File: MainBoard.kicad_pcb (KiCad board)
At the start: 4 copper layers, 150 x 100 mm, 143 parts, among them IC2 STUSB4500LQTR, IC3 RT8293BHZSP, IC4 RT8293BHZSP, J15 USB_C_2.0, J4 Conn_01x06_Pin, J7 IEC61076-2_M8_B-coding_01x03_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, Q6 STL9P3LLH6, Q7 STL9P3LLH6, U1 STM32H723ZGT6, U27 USBLC6-2P6, U4 CA-IS2062W, U51 24AA02-OT, Y5 12M, Y6 32,768kHz

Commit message: I/O Schematic rebuild from DRAFT by Nathann
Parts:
- added C156: 10u/25V/X5R, Capacitor_SMD:C_0805_2012Metric, F.Cu at (83.1, 110.4)
- added L16: 1u/5A, Inductor_SMD:L_APV_APH0650, F.Cu at (80.3, 116.0)
- added U10: VND7050AJTR, Package_SO:PowerSSO-16-1EP_3.9x4.9mm_P0.5mm_EP2.5x3.61mm, F.Cu at (252.6, 58.1)
- added U11: VND7050AJTR, Package_SO:PowerSSO-16-1EP_3.9x4.9mm_P0.5mm_EP2.5x3.61mm, F.Cu at (252.6, 64.5)
- added U12: VND7050AJTR, Package_SO:PowerSSO-16-1EP_3.9x4.9mm_P0.5mm_EP2.5x3.61mm, F.Cu at (252.6, 71.0)
- added U13: VND7050AJTR, Package_SO:PowerSSO-16-1EP_3.9x4.9mm_P0.5mm_EP2.5x3.61mm, F.Cu at (252.6, 77.4)
- added U14: VND7050AJTR, Package_SO:PowerSSO-16-1EP_3.9x4.9mm_P0.5mm_EP2.5x3.61mm, F.Cu at (252.6, 83.9)
- added U15: VND7050AJTR, Package_SO:PowerSSO-16-1EP_3.9x4.9mm_P0.5mm_EP2.5x3.61mm, F.Cu at (273.3, 58.1)
- added U3: VND7050AJTR, Package_SO:PowerSSO-16-1EP_3.9x4.9mm_P0.5mm_EP2.5x3.61mm, F.Cu at (262.9, 51.6)
- added U5: VND7050AJTR, Package_SO:PowerSSO-16-1EP_3.9x4.9mm_P0.5mm_EP2.5x3.61mm, F.Cu at (262.9, 58.1)
- added U6: VND7050AJTR, Package_SO:PowerSSO-16-1EP_3.9x4.9mm_P0.5mm_EP2.5x3.61mm, F.Cu at (262.9, 64.5)
- added U7: VND7050AJTR, Package_SO:PowerSSO-16-1EP_3.9x4.9mm_P0.5mm_EP2.5x3.61mm, F.Cu at (262.9, 71.0)
- added U8: VND7050AJTR, Package_SO:PowerSSO-16-1EP_3.9x4.9mm_P0.5mm_EP2.5x3.61mm, F.Cu at (273.3, 51.6)
- added U9: VND7050AJTR, Package_SO:PowerSSO-16-1EP_3.9x4.9mm_P0.5mm_EP2.5x3.61mm, F.Cu at (252.6, 51.6)
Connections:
- net /USB_PD/USB_N renamed /MCU/USB_N
- net /USB_PD/USB_P renamed /MCU/USB_P
- net /USB_PD/USB_PD_ALERT renamed /MCU/USB_PD_ALERT
- net /USB_PD/USB_PD_RST renamed /MCU/USB_PD_RST
- C134 pad 1: +12V -> Net-(IC3-VIN)
- C269 pad 1: unconnected-(C269-Pad1) -> Net-(U1PortG_PORTH-PC15)
- C270 pad 1: unconnected-(C270-Pad1) -> Net-(U1PortG_PORTH-PC14)
- IC2 pad 7: /USB_PD/I2C2.SCK -> /MCU/I2C2.SCK
- IC2 pad 8: /USB_PD/I2C2.DATA -> /MCU/I2C2.DATA
- IC3 pad 2: +12V -> Net-(IC3-VIN)
- L15 pad 2: +5V -> +12V
- R148 pad 1: +12V -> Net-(IC3-VIN)
- TP22 pad 1: /USB_PD/I2C2.SCK -> /MCU/I2C2.SCK
- TP23 pad 1: /USB_PD/I2C2.DATA -> /MCU/I2C2.DATA
- U1 pad 8: unconnected-(U1PortG_PORTH-PC14-Pad8) -> Net-(U1PortG_PORTH-PC14)
- U1 pad 9: unconnected-(U1PortG_PORTH-PC15-Pad9) -> Net-(U1PortG_PORTH-PC15)
- U4 pad 3: unconnected-(U4-TX-Pad3) -> /PowertrainInterface/CAN1.TX
- U4 pad 5: unconnected-(U4-RX-Pad5) -> /PowertrainInterface/CAN1.RX
- Y6 pad 1: unconnected-(Y6-Pad1) -> Net-(U1PortG_PORTH-PC15)
- Y6 pad 2: unconnected-(Y6-Pad2) -> Net-(U1PortG_PORTH-PC14)
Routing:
- net /MCU/I2C2.DATA: track 19.4 -> 38.0 mm, vias 2 -> 3
- net /USB_PD/I2C2.DATA: track 18.6 -> 0.00 mm, vias 1 -> 0
- net (no net): track 33.4 -> 16.8 mm
- net /USB_PD/I2C2.SCK: track 16.2 -> 0.00 mm, vias 1 -> 0
- net /MCU/I2C2.SCK: track 13.7 -> 29.9 mm, vias 2 -> 3
- net Net-(U1PortG_PORTH-PC15): track 0.00 -> 8.46 mm
- net Net-(U1PortG_PORTH-PC14): track 0.00 -> 8.21 mm
- net Net-(IC3-VIN): track 0.00 -> 4.23 mm, vias 0 -> 1
- net +5V: track 26.3 -> 23.1 mm
- net +12V: track 4.23 -> 3.16 mm, vias 1 -> 0

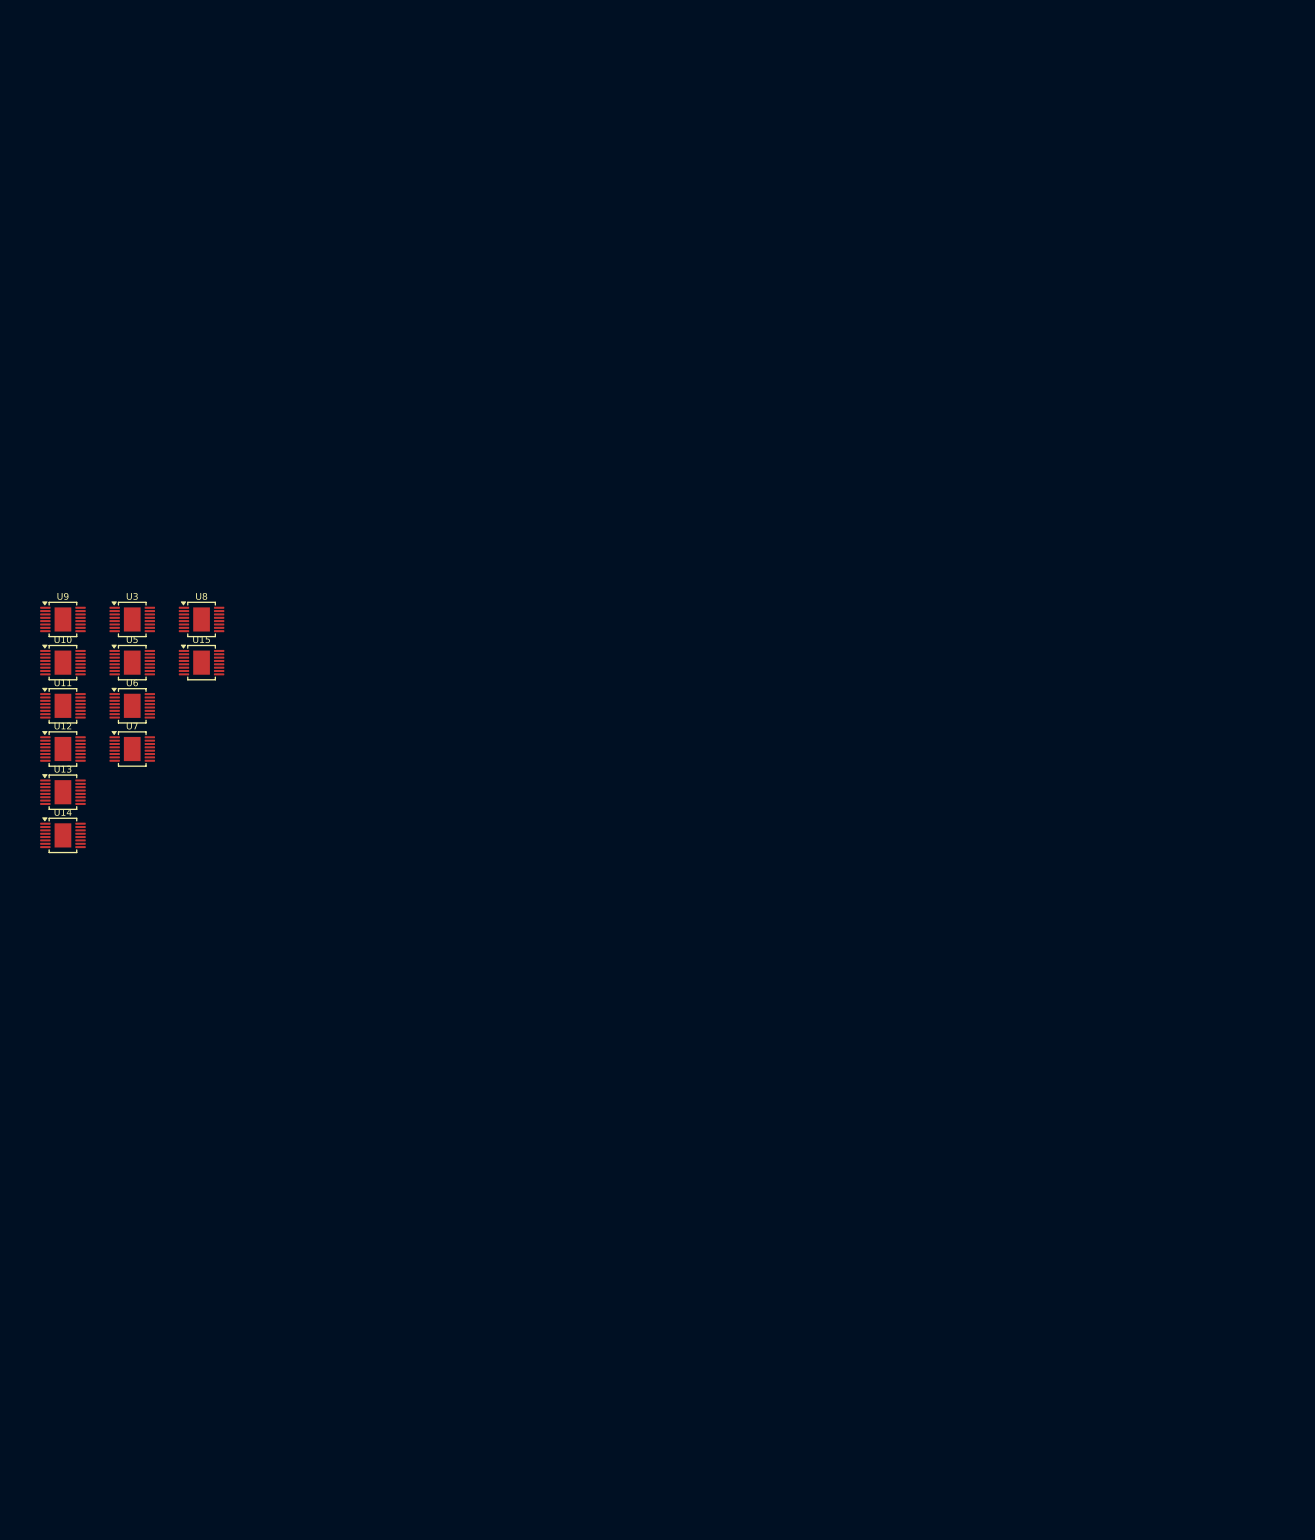
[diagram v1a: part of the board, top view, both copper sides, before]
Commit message: EMI/EMC meassures implementation + VCU panel interface block
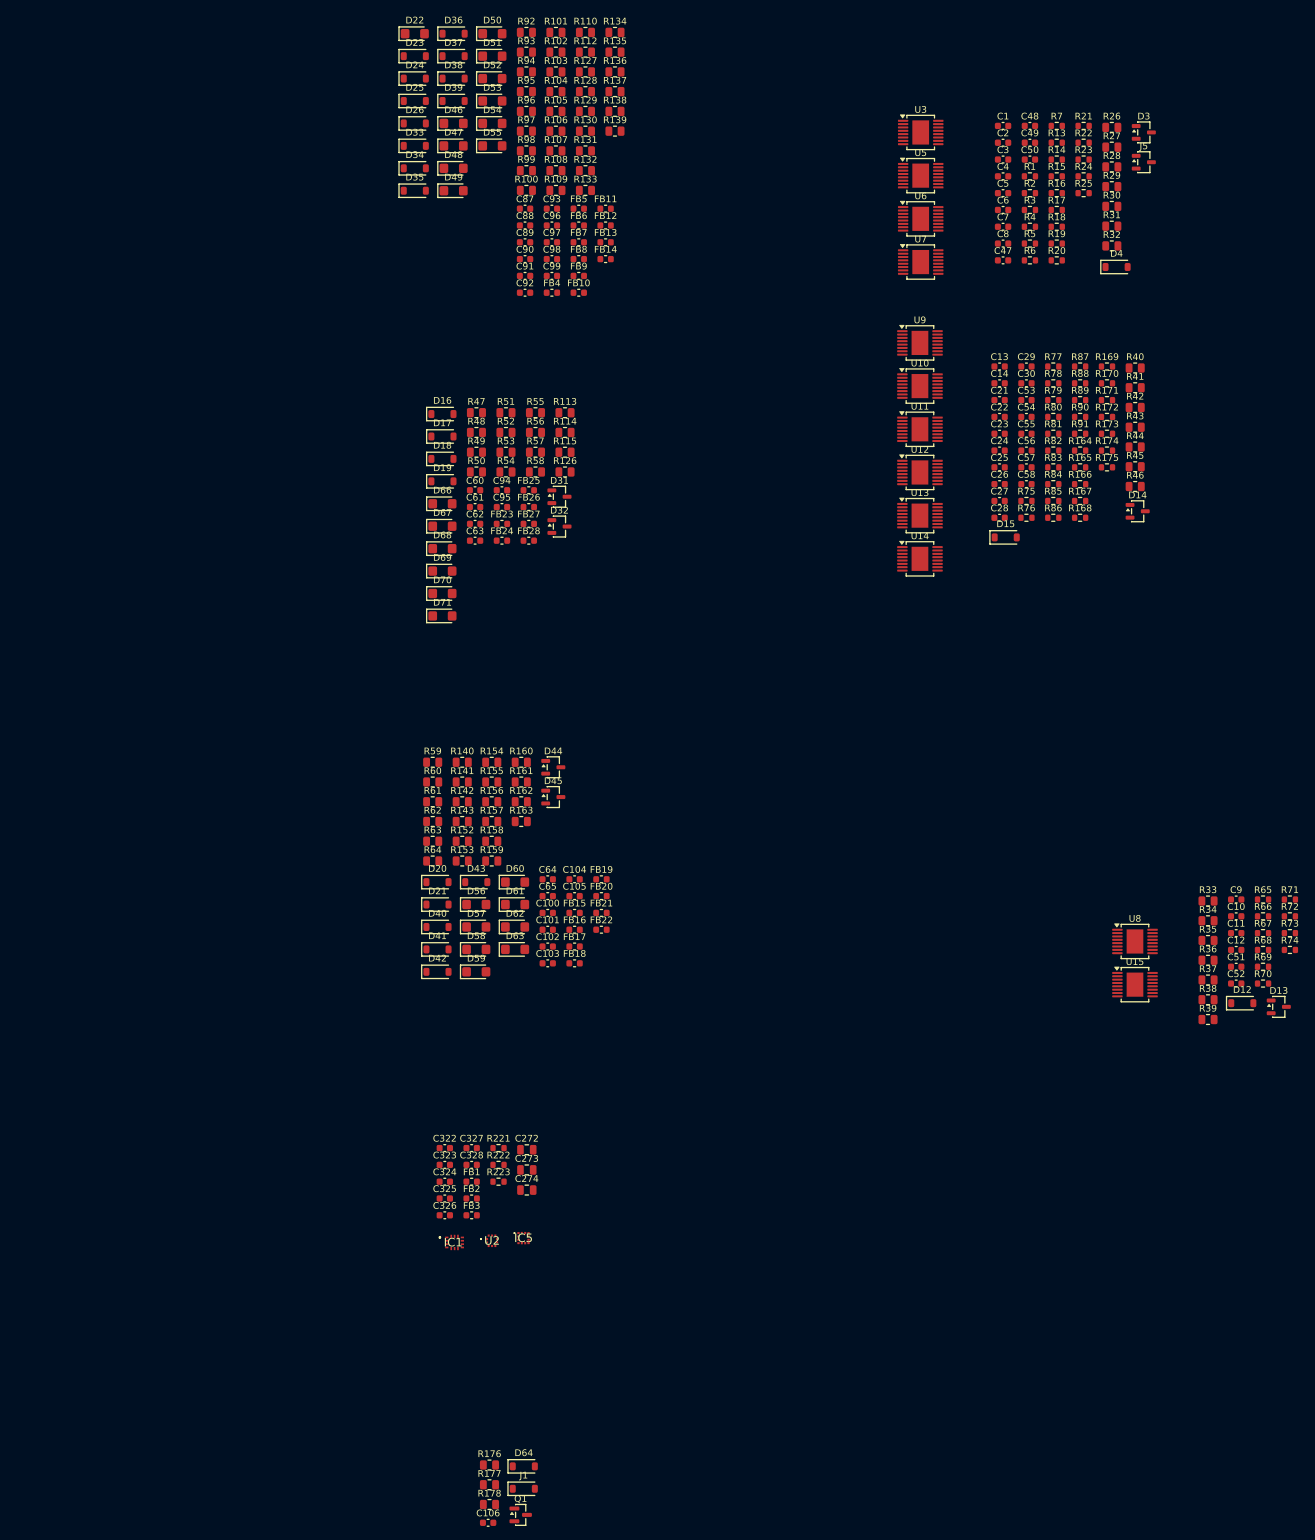
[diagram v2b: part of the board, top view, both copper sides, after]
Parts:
- added C1: 1n, VELION_VCU_Library:C_0603_1608Metric, F.Cu at (393.0, -22.1)
- added C10: 1n, VELION_VCU_Library:C_0603_1608Metric, F.Cu at (427.8, 96.0)
- added C100: 470nF, VELION_VCU_Library:C_0603_1608Metric, F.Cu at (325.0, 95.5)
- added C101: 470nF, VELION_VCU_Library:C_0603_1608Metric, F.Cu at (325.0, 98.0)
- added C102: 470nF, VELION_VCU_Library:C_0603_1608Metric, F.Cu at (325.0, 100.5)
- added C103: 470nF, VELION_VCU_Library:C_0603_1608Metric, F.Cu at (325.0, 103.0)
- added C104: 100nF, VELION_VCU_Library:C_0603_1608Metric, F.Cu at (329.0, 90.4)
- added C105: 100nF, VELION_VCU_Library:C_0603_1608Metric, F.Cu at (329.0, 92.9)
- added C106: 470nF, VELION_VCU_Library:C_0603_1608Metric, F.Cu at (316.1, 186.5)
- added C11: 1n, VELION_VCU_Library:C_0603_1608Metric, F.Cu at (427.8, 98.5)
- added C12: 1n, VELION_VCU_Library:C_0603_1608Metric, F.Cu at (427.8, 101.0)
- added C13: 1n, VELION_VCU_Library:C_0603_1608Metric, F.Cu at (392.5, 13.8)
- added C14: 1n, VELION_VCU_Library:C_0603_1608Metric, F.Cu at (392.5, 16.4)
- added C2: 1n, VELION_VCU_Library:C_0603_1608Metric, F.Cu at (393.0, -19.6)
- added C21: 1n, VELION_VCU_Library:C_0603_1608Metric, F.Cu at (392.5, 18.9)
- added C22: 1n, VELION_VCU_Library:C_0603_1608Metric, F.Cu at (392.5, 21.4)
- added C23: 1n, VELION_VCU_Library:C_0603_1608Metric, F.Cu at (392.5, 23.9)
- added C24: 1n, VELION_VCU_Library:C_0603_1608Metric, F.Cu at (392.5, 26.4)
- added C25: 1n, VELION_VCU_Library:C_0603_1608Metric, F.Cu at (392.5, 28.9)
- added C26: 1n, VELION_VCU_Library:C_0603_1608Metric, F.Cu at (392.5, 31.4)
- added C27: 1n, VELION_VCU_Library:C_0603_1608Metric, F.Cu at (392.5, 33.9)
- added C272: 10u/16V/X7R, VELION_VCU_Library:C_0805_2012Metric, F.Cu at (321.9, 130.8)
- added C273: 10u/16V/X7R, VELION_VCU_Library:C_0805_2012Metric, F.Cu at (321.9, 133.8)
- added C274: 10u/16V/X7R, VELION_VCU_Library:C_0805_2012Metric, F.Cu at (321.9, 136.8)
- added C28: 1n, VELION_VCU_Library:C_0603_1608Metric, F.Cu at (392.5, 36.4)
- added C29: 1n, VELION_VCU_Library:C_0603_1608Metric, F.Cu at (396.5, 13.8)
- added C3: 1n, VELION_VCU_Library:C_0603_1608Metric, F.Cu at (393.0, -17.1)
- added C30: 1n, VELION_VCU_Library:C_0603_1608Metric, F.Cu at (396.5, 16.4)
- added C322: 0u1, VELION_VCU_Library:C_0603_1608Metric, F.Cu at (309.6, 130.6)
- added C323: 0u1, VELION_VCU_Library:C_0603_1608Metric, F.Cu at (309.6, 133.1)
- added C324: 0u1, VELION_VCU_Library:C_0603_1608Metric, F.Cu at (309.6, 135.6)
- added C325: 0u1, VELION_VCU_Library:C_0603_1608Metric, F.Cu at (309.6, 138.1)
- added C326: 0u1, VELION_VCU_Library:C_0603_1608Metric, F.Cu at (309.6, 140.6)
- added C327: 0u1, VELION_VCU_Library:C_0603_1608Metric, F.Cu at (313.6, 130.6)
- added C328: 0u22, VELION_VCU_Library:C_0603_1608Metric, F.Cu at (313.6, 133.1)
- added C4: 1n, VELION_VCU_Library:C_0603_1608Metric, F.Cu at (393.0, -14.6)
- added C47: 100nF, VELION_VCU_Library:C_0603_1608Metric, F.Cu at (393.0, -2.00)
- added C48: 100nF, VELION_VCU_Library:C_0603_1608Metric, F.Cu at (397.0, -22.1)
- added C49: 100nF, VELION_VCU_Library:C_0603_1608Metric, F.Cu at (397.0, -19.6)
- added C5: 1n, VELION_VCU_Library:C_0603_1608Metric, F.Cu at (393.0, -12.0)
- added C50: 100nF, VELION_VCU_Library:C_0603_1608Metric, F.Cu at (397.0, -17.1)
- added C51: 100nF, VELION_VCU_Library:C_0603_1608Metric, F.Cu at (427.8, 103.5)
- added C52: 100nF, VELION_VCU_Library:C_0603_1608Metric, F.Cu at (427.8, 106.0)
- added C53: 100nF, VELION_VCU_Library:C_0603_1608Metric, F.Cu at (396.5, 18.9)
- added C54: 100nF, VELION_VCU_Library:C_0603_1608Metric, F.Cu at (396.5, 21.4)
- added C55: 100nF, VELION_VCU_Library:C_0603_1608Metric, F.Cu at (396.5, 23.9)
- added C56: 100nF, VELION_VCU_Library:C_0603_1608Metric, F.Cu at (396.5, 26.4)
- added C57: 100nF, VELION_VCU_Library:C_0603_1608Metric, F.Cu at (396.5, 28.9)
- added C58: 100nF, VELION_VCU_Library:C_0603_1608Metric, F.Cu at (396.5, 31.4)
- added C6: 1n, VELION_VCU_Library:C_0603_1608Metric, F.Cu at (393.0, -9.53)
- added C60: 100nF, VELION_VCU_Library:C_0603_1608Metric, F.Cu at (314.1, 32.3)
- added C61: 100nF, VELION_VCU_Library:C_0603_1608Metric, F.Cu at (314.1, 34.8)
- added C62: 100nF, VELION_VCU_Library:C_0603_1608Metric, F.Cu at (314.1, 37.4)
- added C63: 100nF, VELION_VCU_Library:C_0603_1608Metric, F.Cu at (314.1, 39.9)
- added C64: 100nF, VELION_VCU_Library:C_0603_1608Metric, F.Cu at (325.0, 90.4)
- added C65: 100nF, VELION_VCU_Library:C_0603_1608Metric, F.Cu at (325.0, 92.9)
- added C7: 1n, VELION_VCU_Library:C_0603_1608Metric, F.Cu at (393.0, -7.02)
- added C8: 1n, VELION_VCU_Library:C_0603_1608Metric, F.Cu at (393.0, -4.51)
- added C87: 470nF, VELION_VCU_Library:C_0603_1608Metric, F.Cu at (321.6, -9.72)
- added C88: 470nF, VELION_VCU_Library:C_0603_1608Metric, F.Cu at (321.6, -7.21)
- added C89: 470nF, VELION_VCU_Library:C_0603_1608Metric, F.Cu at (321.6, -4.70)
- added C9: 1n, VELION_VCU_Library:C_0603_1608Metric, F.Cu at (427.8, 93.5)
- added C90: 470nF, VELION_VCU_Library:C_0603_1608Metric, F.Cu at (321.6, -2.19)
- added C91: 470nF, VELION_VCU_Library:C_0603_1608Metric, F.Cu at (321.6, 0.32)
- added C92: 470nF, VELION_VCU_Library:C_0603_1608Metric, F.Cu at (321.6, 2.83)
- added C93: 470nF, VELION_VCU_Library:C_0603_1608Metric, F.Cu at (325.6, -9.72)
- added C94: 100nF, VELION_VCU_Library:C_0603_1608Metric, F.Cu at (318.1, 32.3)
- added C95: 100nF, VELION_VCU_Library:C_0603_1608Metric, F.Cu at (318.1, 34.8)
- added C96: 470nF, VELION_VCU_Library:C_0603_1608Metric, F.Cu at (325.6, -7.21)
- added C97: 470nF, VELION_VCU_Library:C_0603_1608Metric, F.Cu at (325.6, -4.70)
- added C98: 470nF, VELION_VCU_Library:C_0603_1608Metric, F.Cu at (325.6, -2.19)
- added C99: 470nF, VELION_VCU_Library:C_0603_1608Metric, F.Cu at (325.6, 0.32)
- added D12: 1N4148W, VELION_VCU_Library:D_SOD-123, F.Cu at (428.7, 108.9)
- added D13: BAT54S_C7420333, VELION_VCU_Library:SOT-23-3, F.Cu at (434.1, 109.5)
- added D14: BAT54S_C7420333, VELION_VCU_Library:SOT-23-3, F.Cu at (413.1, 35.5)
- added D15: 1N4148W, VELION_VCU_Library:D_SOD-123, F.Cu at (393.4, 39.4)
- added D16: 1N4148W, VELION_VCU_Library:D_SOD-123, F.Cu at (309.2, 20.9)
- added D17: 1N4148W, VELION_VCU_Library:D_SOD-123, F.Cu at (309.2, 24.3)
- added D18: 1N4148W, VELION_VCU_Library:D_SOD-123, F.Cu at (309.2, 27.6)
- added D19: 1N4148W, VELION_VCU_Library:D_SOD-123, F.Cu at (309.2, 31.0)
- added D20: 1N4148W, VELION_VCU_Library:D_SOD-123, F.Cu at (308.5, 90.8)
- added D21: 1N4148W, VELION_VCU_Library:D_SOD-123, F.Cu at (308.5, 94.2)
- added D22: SMF13A, VELION_VCU_Library:D_SMF, F.Cu at (305.1, -35.9)
- added D23: 1N4148W, VELION_VCU_Library:D_SOD-123, F.Cu at (305.1, -32.5)
- added D24: 1N4148W, VELION_VCU_Library:D_SOD-123, F.Cu at (305.1, -29.1)
- added D25: 1N4148W, VELION_VCU_Library:D_SOD-123, F.Cu at (305.1, -25.8)
- added D26: 1N4148W, VELION_VCU_Library:D_SOD-123, F.Cu at (305.1, -22.4)
- added D3: BAT54S_C7420333, VELION_VCU_Library:SOT-23-3, F.Cu at (414.0, -21.1)
- added D31: BAT54S_C7420333, VELION_VCU_Library:SOT-23-3, F.Cu at (326.7, 33.3)
- added D32: BAT54S_C7420333, VELION_VCU_Library:SOT-23-3, F.Cu at (326.7, 37.8)
- added D33: 1N4148W, VELION_VCU_Library:D_SOD-123, F.Cu at (305.1, -19.1)
- added D34: 1N4148W, VELION_VCU_Library:D_SOD-123, F.Cu at (305.1, -15.8)
- added D35: 1N4148W, VELION_VCU_Library:D_SOD-123, F.Cu at (305.1, -12.4)
- added D36: 1N4148W, VELION_VCU_Library:D_SOD-123, F.Cu at (310.9, -35.9)
- added D37: 1N4148W, VELION_VCU_Library:D_SOD-123, F.Cu at (310.9, -32.5)
- added D38: 1N4148W, VELION_VCU_Library:D_SOD-123, F.Cu at (310.9, -29.1)
- added D39: 1N4148W, VELION_VCU_Library:D_SOD-123, F.Cu at (310.9, -25.8)
- added D4: 1N4148W, VELION_VCU_Library:D_SOD-123, F.Cu at (409.9, -1.01)
- added D40: 1N4148W, VELION_VCU_Library:D_SOD-123, F.Cu at (308.5, 97.5)
- added D41: 1N4148W, VELION_VCU_Library:D_SOD-123, F.Cu at (308.5, 100.9)
- added D42: 1N4148W, VELION_VCU_Library:D_SOD-123, F.Cu at (308.5, 104.2)
- added D43: 1N4148W, VELION_VCU_Library:D_SOD-123, F.Cu at (314.3, 90.8)
- added D44: BAT54S_C7420333, VELION_VCU_Library:SOT-23-3, F.Cu at (325.8, 73.7)
- added D45: BAT54S_C7420333, VELION_VCU_Library:SOT-23-3, F.Cu at (325.8, 78.2)
- added D46: SMF13A, VELION_VCU_Library:D_SMF, F.Cu at (310.9, -22.4)
- added D47: SMF13A, VELION_VCU_Library:D_SMF, F.Cu at (310.9, -19.1)
- added D48: SMF13A, VELION_VCU_Library:D_SMF, F.Cu at (310.9, -15.8)
- added D49: SMF13A, VELION_VCU_Library:D_SMF, F.Cu at (310.9, -12.4)
- added D50: SMF13A, VELION_VCU_Library:D_SMF, F.Cu at (316.7, -35.9)
- added D51: SMF13A, VELION_VCU_Library:D_SMF, F.Cu at (316.7, -32.5)
- added D52: SMF13A, VELION_VCU_Library:D_SMF, F.Cu at (316.7, -29.1)
- added D53: SMF13A, VELION_VCU_Library:D_SMF, F.Cu at (316.7, -25.8)
- added D54: SMF13A, VELION_VCU_Library:D_SMF, F.Cu at (316.7, -22.4)
- added D55: SMF13A, VELION_VCU_Library:D_SMF, F.Cu at (316.7, -19.1)
- added D56: SMF13A, VELION_VCU_Library:D_SMF, F.Cu at (314.3, 94.2)
- added D57: SMF13A, VELION_VCU_Library:D_SMF, F.Cu at (314.3, 97.5)
- added D58: SMF13A, VELION_VCU_Library:D_SMF, F.Cu at (314.3, 100.9)
- added D59: SMF6V0A, VELION_VCU_Library:D_SMF, F.Cu at (314.3, 104.2)
- added D60: SMF6V0A, VELION_VCU_Library:D_SMF, F.Cu at (320.1, 90.8)
- added D61: SMF6V0A, VELION_VCU_Library:D_SMF, F.Cu at (320.1, 94.2)
- added D62: SMF6V0A, VELION_VCU_Library:D_SMF, F.Cu at (320.1, 97.5)
- added D63: SMF13A, VELION_VCU_Library:D_SMF, F.Cu at (320.1, 100.9)
- added D64: 1N4148W, VELION_VCU_Library:D_SOD-123, F.Cu at (321.4, 178.1)
- added D66: SMF13A, VELION_VCU_Library:D_SMF, F.Cu at (309.2, 34.4)
- added D67: SMF13A, VELION_VCU_Library:D_SMF, F.Cu at (309.2, 37.7)
- added D68: SMF6V0A, VELION_VCU_Library:D_SMF, F.Cu at (309.2, 41.0)
- added D69: SMF6V0A, VELION_VCU_Library:D_SMF, F.Cu at (309.2, 44.4)
- added D70: SMF6V0A, VELION_VCU_Library:D_SMF, F.Cu at (309.2, 47.8)
- added D71: SMF6V0A, VELION_VCU_Library:D_SMF, F.Cu at (309.2, 51.1)
- added FB1: FerriteBead_Small, VELION_VCU_Library:L_0603_1608Metric, F.Cu at (313.6, 135.6)
- added FB10: 100R, VELION_VCU_Library:L_0603_1608Metric, F.Cu at (329.6, 2.83)
- added FB11: 100R, VELION_VCU_Library:L_0603_1608Metric, F.Cu at (333.6, -9.72)
- added FB12: 100R, VELION_VCU_Library:L_0603_1608Metric, F.Cu at (333.6, -7.21)
- added FB13: 100R, VELION_VCU_Library:L_0603_1608Metric, F.Cu at (333.6, -4.70)
- added FB14: 100R, VELION_VCU_Library:L_0603_1608Metric, F.Cu at (333.6, -2.19)
- added FB15: 100R, VELION_VCU_Library:L_0603_1608Metric, F.Cu at (329.0, 95.5)
- added FB16: 100R, VELION_VCU_Library:L_0603_1608Metric, F.Cu at (329.0, 98.0)
- added FB17: 100R, VELION_VCU_Library:L_0603_1608Metric, F.Cu at (329.0, 100.5)
- added FB18: 100R, VELION_VCU_Library:L_0603_1608Metric, F.Cu at (329.0, 103.0)
- added FB19: 100R, VELION_VCU_Library:L_0603_1608Metric, F.Cu at (333.0, 90.4)
- added FB2: FerriteBead_Small, VELION_VCU_Library:L_0603_1608Metric, F.Cu at (313.6, 138.1)
- added FB20: 100R, VELION_VCU_Library:L_0603_1608Metric, F.Cu at (333.0, 92.9)
- added FB21: 100R, VELION_VCU_Library:L_0603_1608Metric, F.Cu at (333.0, 95.5)
- added FB22: 100R, VELION_VCU_Library:L_0603_1608Metric, F.Cu at (333.0, 98.0)
- added FB23: 100R, VELION_VCU_Library:L_0603_1608Metric, F.Cu at (318.1, 37.4)
- added FB24: 100R, VELION_VCU_Library:L_0603_1608Metric, F.Cu at (318.1, 39.9)
- added FB25: 100R, VELION_VCU_Library:L_0603_1608Metric, F.Cu at (322.1, 32.3)
- added FB26: 100R, VELION_VCU_Library:L_0603_1608Metric, F.Cu at (322.1, 34.8)
- added FB27: 100R, VELION_VCU_Library:L_0603_1608Metric, F.Cu at (322.1, 37.4)
- added FB28: 100R, VELION_VCU_Library:L_0603_1608Metric, F.Cu at (322.1, 39.9)
- added FB3: FerriteBead_Small, VELION_VCU_Library:L_0603_1608Metric, F.Cu at (313.6, 140.6)
- added FB4: 100R, VELION_VCU_Library:L_0603_1608Metric, F.Cu at (325.6, 2.83)
- added FB5: 100R, VELION_VCU_Library:L_0603_1608Metric, F.Cu at (329.6, -9.72)
- added FB6: 100R, VELION_VCU_Library:L_0603_1608Metric, F.Cu at (329.6, -7.21)
- added FB7: 100R, VELION_VCU_Library:L_0603_1608Metric, F.Cu at (329.6, -4.70)
- added FB8: 100R, VELION_VCU_Library:L_0603_1608Metric, F.Cu at (329.6, -2.19)
- added FB9: 100R, VELION_VCU_Library:L_0603_1608Metric, F.Cu at (329.6, 0.32)
- added IC1: ASM330LHHTR, VELION_VCU_Library:LSM6DS3USTR, F.Cu at (311.1, 144.7)
- added IC5: IIS2MDCTR, VELION_VCU_Library:IIS2MDCTR, F.Cu at (321.4, 144.0)
- added J1: Conn_01x04, VELION_VCU_Library:D_SOD-123, F.Cu at (321.4, 181.4)
- added J5: Conn_01x09, VELION_VCU_Library:SOT-23-3, F.Cu at (414.0, -16.7)
- added Q1: DTC123Y, VELION_VCU_Library:SOT-23, F.Cu at (320.9, 185.3)
- added R1: 1k, VELION_VCU_Library:R_0603_1608Metric, F.Cu at (397.0, -14.6)
- added R100: 1.2kΩ, VELION_VCU_Library:R_0805_2012Metric, F.Cu at (321.8, -12.4)
- added R101: 10kΩ, VELION_VCU_Library:R_0805_2012Metric, F.Cu at (326.2, -36.0)
- added R102: 33kΩ, VELION_VCU_Library:R_0805_2012Metric, F.Cu at (326.2, -33.1)
- added R103: 1.2kΩ, VELION_VCU_Library:R_0805_2012Metric, F.Cu at (326.2, -30.1)
- added R104: 10kΩ, VELION_VCU_Library:R_0805_2012Metric, F.Cu at (326.2, -27.2)
- added R105: 33kΩ, VELION_VCU_Library:R_0805_2012Metric, F.Cu at (326.2, -24.2)
- added R106: 1.2kΩ, VELION_VCU_Library:R_0805_2012Metric, F.Cu at (326.2, -21.3)
- added R107: 10kΩ, VELION_VCU_Library:R_0805_2012Metric, F.Cu at (326.2, -18.4)
- added R108: 33kΩ, VELION_VCU_Library:R_0805_2012Metric, F.Cu at (326.2, -15.4)
- added R109: 1.2kΩ, VELION_VCU_Library:R_0805_2012Metric, F.Cu at (326.2, -12.4)
- added R110: 10kΩ, VELION_VCU_Library:R_0805_2012Metric, F.Cu at (330.6, -36.0)
- added R112: 33kΩ, VELION_VCU_Library:R_0805_2012Metric, F.Cu at (330.6, -33.1)
- added R113: 10kΩ, VELION_VCU_Library:R_0805_2012Metric, F.Cu at (327.6, 20.8)
- added R114: 15kΩ, VELION_VCU_Library:R_0805_2012Metric, F.Cu at (327.6, 23.7)
- added R115: 10kΩ, VELION_VCU_Library:R_0805_2012Metric, F.Cu at (327.6, 26.6)
- added R126: 15kΩ, VELION_VCU_Library:R_0805_2012Metric, F.Cu at (327.6, 29.6)
- added R127: 1.2kΩ, VELION_VCU_Library:R_0805_2012Metric, F.Cu at (330.6, -30.1)
- added R128: 10kΩ, VELION_VCU_Library:R_0805_2012Metric, F.Cu at (330.6, -27.2)
- added R129: 33kΩ, VELION_VCU_Library:R_0805_2012Metric, F.Cu at (330.6, -24.2)
- added R13: 1k, VELION_VCU_Library:R_0603_1608Metric, F.Cu at (401.0, -19.6)
- added R130: 1.2kΩ, VELION_VCU_Library:R_0805_2012Metric, F.Cu at (330.6, -21.3)
- added R131: 10kΩ, VELION_VCU_Library:R_0805_2012Metric, F.Cu at (330.6, -18.4)
- added R132: 33kΩ, VELION_VCU_Library:R_0805_2012Metric, F.Cu at (330.6, -15.4)
- added R133: 1.2kΩ, VELION_VCU_Library:R_0805_2012Metric, F.Cu at (330.6, -12.4)
- added R134: 10kΩ, VELION_VCU_Library:R_0805_2012Metric, F.Cu at (335.0, -36.0)
- added R135: 33kΩ, VELION_VCU_Library:R_0805_2012Metric, F.Cu at (335.0, -33.1)
- added R136: 1.2kΩ, VELION_VCU_Library:R_0805_2012Metric, F.Cu at (335.0, -30.1)
- added R137: 10kΩ, VELION_VCU_Library:R_0805_2012Metric, F.Cu at (335.0, -27.2)
- added R138: 33kΩ, VELION_VCU_Library:R_0805_2012Metric, F.Cu at (335.0, -24.2)
- added R139: 1.2kΩ, VELION_VCU_Library:R_0805_2012Metric, F.Cu at (335.0, -21.3)
- added R14: 1k, VELION_VCU_Library:R_0603_1608Metric, F.Cu at (401.0, -17.1)
- added R140: 10kΩ, VELION_VCU_Library:R_0805_2012Metric, F.Cu at (312.2, 73.0)
- added R141: 33kΩ, VELION_VCU_Library:R_0805_2012Metric, F.Cu at (312.2, 75.9)
- added R142: 1.2kΩ, VELION_VCU_Library:R_0805_2012Metric, F.Cu at (312.2, 78.8)
- added R143: 10kΩ, VELION_VCU_Library:R_0805_2012Metric, F.Cu at (312.2, 81.8)
- added R15: 1k, VELION_VCU_Library:R_0603_1608Metric, F.Cu at (401.0, -14.6)
- added R152: 33kΩ, VELION_VCU_Library:R_0805_2012Metric, F.Cu at (312.2, 84.8)
- added R153: 1.2kΩ, VELION_VCU_Library:R_0805_2012Metric, F.Cu at (312.2, 87.7)
- added R154: 10kΩ, VELION_VCU_Library:R_0805_2012Metric, F.Cu at (316.6, 73.0)
- added R155: 33kΩ, VELION_VCU_Library:R_0805_2012Metric, F.Cu at (316.6, 75.9)
- added R156: 1.2kΩ, VELION_VCU_Library:R_0805_2012Metric, F.Cu at (316.6, 78.8)
- added R157: 10kΩ, VELION_VCU_Library:R_0805_2012Metric, F.Cu at (316.6, 81.8)
- added R158: 33kΩ, VELION_VCU_Library:R_0805_2012Metric, F.Cu at (316.6, 84.8)
- added R159: 1.2kΩ, VELION_VCU_Library:R_0805_2012Metric, F.Cu at (316.6, 87.7)
- added R16: 1k, VELION_VCU_Library:R_0603_1608Metric, F.Cu at (401.0, -12.0)
- added R160: 10kΩ, VELION_VCU_Library:R_0805_2012Metric, F.Cu at (321.0, 73.0)
- added R161: 15kΩ, VELION_VCU_Library:R_0805_2012Metric, F.Cu at (321.0, 75.9)
- added R162: 10kΩ, VELION_VCU_Library:R_0805_2012Metric, F.Cu at (321.0, 78.8)
- added R163: 15kΩ, VELION_VCU_Library:R_0805_2012Metric, F.Cu at (321.0, 81.8)
- added R164: 1k, VELION_VCU_Library:R_0603_1608Metric, F.Cu at (404.5, 26.4)
- added R165: 1k, VELION_VCU_Library:R_0603_1608Metric, F.Cu at (404.5, 28.9)
- added R166: 1k, VELION_VCU_Library:R_0603_1608Metric, F.Cu at (404.5, 31.4)
- added R167: 1k, VELION_VCU_Library:R_0603_1608Metric, F.Cu at (404.5, 33.9)
- added R168: 1k, VELION_VCU_Library:R_0603_1608Metric, F.Cu at (404.5, 36.4)
- added R169: 1k, VELION_VCU_Library:R_0603_1608Metric, F.Cu at (408.5, 13.8)
- added R17: 1k, VELION_VCU_Library:R_0603_1608Metric, F.Cu at (401.0, -9.53)
- added R170: 1k, VELION_VCU_Library:R_0603_1608Metric, F.Cu at (408.5, 16.4)
- added R171: 1k, VELION_VCU_Library:R_0603_1608Metric, F.Cu at (408.5, 18.9)
- added R172: 1k, VELION_VCU_Library:R_0603_1608Metric, F.Cu at (408.5, 21.4)
- added R173: 1k, VELION_VCU_Library:R_0603_1608Metric, F.Cu at (408.5, 23.9)
- added R174: 1k, VELION_VCU_Library:R_0603_1608Metric, F.Cu at (408.5, 26.4)
- added R175: 1k, VELION_VCU_Library:R_0603_1608Metric, F.Cu at (408.5, 28.9)
- added R176: 10kΩ, VELION_VCU_Library:R_0805_2012Metric, F.Cu at (316.3, 177.9)
- added R177: 33kΩ, VELION_VCU_Library:R_0805_2012Metric, F.Cu at (316.3, 180.8)
- added R178: 1.2kΩ, VELION_VCU_Library:R_0805_2012Metric, F.Cu at (316.3, 183.8)
- added R18: 22R, VELION_VCU_Library:R_0603_1608Metric, F.Cu at (401.0, -7.02)
- added R19: 22R, VELION_VCU_Library:R_0603_1608Metric, F.Cu at (401.0, -4.51)
- added R2: 1k, VELION_VCU_Library:R_0603_1608Metric, F.Cu at (397.0, -12.0)
- added R20: 22R, VELION_VCU_Library:R_0603_1608Metric, F.Cu at (401.0, -2.00)
- added R21: 22R, VELION_VCU_Library:R_0603_1608Metric, F.Cu at (405.0, -22.1)
- added R22: 22R, VELION_VCU_Library:R_0603_1608Metric, F.Cu at (405.0, -19.6)
- added R221: 2k2, VELION_VCU_Library:R_0603_1608Metric, F.Cu at (317.6, 130.6)
- added R222: 0R, VELION_VCU_Library:R_0603_1608Metric, F.Cu at (317.6, 133.1)
- added R223: 0R, VELION_VCU_Library:R_0603_1608Metric, F.Cu at (317.6, 135.6)
- added R23: 22R, VELION_VCU_Library:R_0603_1608Metric, F.Cu at (405.0, -17.1)
- added R24: 22R, VELION_VCU_Library:R_0603_1608Metric, F.Cu at (405.0, -14.6)
- added R25: 22R, VELION_VCU_Library:R_0603_1608Metric, F.Cu at (405.0, -12.0)
- added R26: 1kΩ, VELION_VCU_Library:R_0805_2012Metric, F.Cu at (409.2, -21.9)
- added R27: 1kΩ, VELION_VCU_Library:R_0805_2012Metric, F.Cu at (409.2, -18.9)
- added R28: 1kΩ, VELION_VCU_Library:R_0805_2012Metric, F.Cu at (409.2, -16.0)
- added R29: 1kΩ, VELION_VCU_Library:R_0805_2012Metric, F.Cu at (409.2, -13.0)
- added R3: 1k, VELION_VCU_Library:R_0603_1608Metric, F.Cu at (397.0, -9.53)
- added R30: 1kΩ, VELION_VCU_Library:R_0805_2012Metric, F.Cu at (409.2, -10.1)
- added R31: 1kΩ, VELION_VCU_Library:R_0805_2012Metric, F.Cu at (409.2, -7.11)
- added R32: 4.7kΩ, VELION_VCU_Library:R_0805_2012Metric, F.Cu at (409.2, -4.16)
- added R33: 4.7kΩ, VELION_VCU_Library:R_0805_2012Metric, F.Cu at (423.6, 93.7)
- added R34: 1kΩ, VELION_VCU_Library:R_0805_2012Metric, F.Cu at (423.6, 96.6)
- added R35: 1kΩ, VELION_VCU_Library:R_0805_2012Metric, F.Cu at (423.6, 99.6)
- added R36: 1kΩ, VELION_VCU_Library:R_0805_2012Metric, F.Cu at (423.6, 102.5)
- added R37: 1kΩ, VELION_VCU_Library:R_0805_2012Metric, F.Cu at (423.6, 105.5)
- added R38: 1kΩ, VELION_VCU_Library:R_0805_2012Metric, F.Cu at (423.6, 108.4)
- added R39: 1kΩ, VELION_VCU_Library:R_0805_2012Metric, F.Cu at (423.6, 111.4)
- added R4: 1k, VELION_VCU_Library:R_0603_1608Metric, F.Cu at (397.0, -7.02)
- added R40: 1kΩ, VELION_VCU_Library:R_0805_2012Metric, F.Cu at (412.7, 14.1)
- added R41: 1kΩ, VELION_VCU_Library:R_0805_2012Metric, F.Cu at (412.7, 17.0)
- added R42: 1kΩ, VELION_VCU_Library:R_0805_2012Metric, F.Cu at (412.7, 20.0)
- added R43: 1kΩ, VELION_VCU_Library:R_0805_2012Metric, F.Cu at (412.7, 22.9)
- added R44: 1kΩ, VELION_VCU_Library:R_0805_2012Metric, F.Cu at (412.7, 25.9)
- added R45: 1kΩ, VELION_VCU_Library:R_0805_2012Metric, F.Cu at (412.7, 28.8)
- added R46: 4.7kΩ, VELION_VCU_Library:R_0805_2012Metric, F.Cu at (412.7, 31.8)
- added R47: 4.7kΩ, VELION_VCU_Library:R_0805_2012Metric, F.Cu at (314.3, 20.8)
- added R48: 10kΩ, VELION_VCU_Library:R_0805_2012Metric, F.Cu at (314.3, 23.7)
- added R49: 20kΩ, VELION_VCU_Library:R_0805_2012Metric, F.Cu at (314.3, 26.6)
- added R5: 1k, VELION_VCU_Library:R_0603_1608Metric, F.Cu at (397.0, -4.51)
- added R50: 4.7kΩ, VELION_VCU_Library:R_0805_2012Metric, F.Cu at (314.3, 29.6)
- added R51: 10kΩ, VELION_VCU_Library:R_0805_2012Metric, F.Cu at (318.7, 20.8)
- added R52: 20kΩ, VELION_VCU_Library:R_0805_2012Metric, F.Cu at (318.7, 23.7)
- added R53: 20kΩ, VELION_VCU_Library:R_0805_2012Metric, F.Cu at (318.7, 26.6)
- added R54: 20kΩ, VELION_VCU_Library:R_0805_2012Metric, F.Cu at (318.7, 29.6)
- added R55: 10kΩ, VELION_VCU_Library:R_0805_2012Metric, F.Cu at (323.1, 20.8)
- added R56: 10kΩ, VELION_VCU_Library:R_0805_2012Metric, F.Cu at (323.1, 23.7)
- added R57: 4.7kΩ, VELION_VCU_Library:R_0805_2012Metric, F.Cu at (323.1, 26.6)
- added R58: 4.7kΩ, VELION_VCU_Library:R_0805_2012Metric, F.Cu at (323.1, 29.6)
- added R59: 20kΩ, VELION_VCU_Library:R_0805_2012Metric, F.Cu at (307.8, 73.0)
- added R6: 1k, VELION_VCU_Library:R_0603_1608Metric, F.Cu at (397.0, -2.00)
- added R60: 20kΩ, VELION_VCU_Library:R_0805_2012Metric, F.Cu at (307.8, 75.9)
- added R61: 10kΩ, VELION_VCU_Library:R_0805_2012Metric, F.Cu at (307.8, 78.8)
- added R62: 10kΩ, VELION_VCU_Library:R_0805_2012Metric, F.Cu at (307.8, 81.8)
- added R63: 4.7kΩ, VELION_VCU_Library:R_0805_2012Metric, F.Cu at (307.8, 84.8)
- added R64: 4.7kΩ, VELION_VCU_Library:R_0805_2012Metric, F.Cu at (307.8, 87.7)
- added R65: 22R, VELION_VCU_Library:R_0603_1608Metric, F.Cu at (431.8, 93.5)
- added R66: 22R, VELION_VCU_Library:R_0603_1608Metric, F.Cu at (431.8, 96.0)
- added R67: 22R, VELION_VCU_Library:R_0603_1608Metric, F.Cu at (431.8, 98.5)
- added R68: 22R, VELION_VCU_Library:R_0603_1608Metric, F.Cu at (431.8, 101.0)
- added R69: 1k, VELION_VCU_Library:R_0603_1608Metric, F.Cu at (431.8, 103.5)
- added R7: 1k, VELION_VCU_Library:R_0603_1608Metric, F.Cu at (401.0, -22.1)
- added R70: 1k, VELION_VCU_Library:R_0603_1608Metric, F.Cu at (431.8, 106.0)
- added R71: 1k, VELION_VCU_Library:R_0603_1608Metric, F.Cu at (435.8, 93.5)
- added R72: 1k, VELION_VCU_Library:R_0603_1608Metric, F.Cu at (435.8, 96.0)
- added R73: 1k, VELION_VCU_Library:R_0603_1608Metric, F.Cu at (435.8, 98.5)
- added R74: 1k, VELION_VCU_Library:R_0603_1608Metric, F.Cu at (435.8, 101.0)
- added R75: 22R, VELION_VCU_Library:R_0603_1608Metric, F.Cu at (396.5, 33.9)
- added R76: 22R, VELION_VCU_Library:R_0603_1608Metric, F.Cu at (396.5, 36.4)
- added R77: 22R, VELION_VCU_Library:R_0603_1608Metric, F.Cu at (400.5, 13.8)
- added R78: 22R, VELION_VCU_Library:R_0603_1608Metric, F.Cu at (400.5, 16.4)
- added R79: 22R, VELION_VCU_Library:R_0603_1608Metric, F.Cu at (400.5, 18.9)
- added R80: 22R, VELION_VCU_Library:R_0603_1608Metric, F.Cu at (400.5, 21.4)
- added R81: 22R, VELION_VCU_Library:R_0603_1608Metric, F.Cu at (400.5, 23.9)
- added R82: 22R, VELION_VCU_Library:R_0603_1608Metric, F.Cu at (400.5, 26.4)
- added R83: 22R, VELION_VCU_Library:R_0603_1608Metric, F.Cu at (400.5, 28.9)
- added R84: 22R, VELION_VCU_Library:R_0603_1608Metric, F.Cu at (400.5, 31.4)
- added R85: 22R, VELION_VCU_Library:R_0603_1608Metric, F.Cu at (400.5, 33.9)
- added R86: 22R, VELION_VCU_Library:R_0603_1608Metric, F.Cu at (400.5, 36.4)
- added R87: 1k, VELION_VCU_Library:R_0603_1608Metric, F.Cu at (404.5, 13.8)
- added R88: 1k, VELION_VCU_Library:R_0603_1608Metric, F.Cu at (404.5, 16.4)
- added R89: 1k, VELION_VCU_Library:R_0603_1608Metric, F.Cu at (404.5, 18.9)
- added R90: 1k, VELION_VCU_Library:R_0603_1608Metric, F.Cu at (404.5, 21.4)
- added R91: 1k, VELION_VCU_Library:R_0603_1608Metric, F.Cu at (404.5, 23.9)
- added R92: 1.2kΩ, VELION_VCU_Library:R_0805_2012Metric, F.Cu at (321.8, -36.0)
- added R93: 33kΩ, VELION_VCU_Library:R_0805_2012Metric, F.Cu at (321.8, -33.1)
- added R94: 10kΩ, VELION_VCU_Library:R_0805_2012Metric, F.Cu at (321.8, -30.1)
- added R95: 10kΩ, VELION_VCU_Library:R_0805_2012Metric, F.Cu at (321.8, -27.2)
- added R96: 33kΩ, VELION_VCU_Library:R_0805_2012Metric, F.Cu at (321.8, -24.2)
- added R97: 1.2kΩ, VELION_VCU_Library:R_0805_2012Metric, F.Cu at (321.8, -21.3)
- added R98: 10kΩ, VELION_VCU_Library:R_0805_2012Metric, F.Cu at (321.8, -18.4)
- added R99: 33kΩ, VELION_VCU_Library:R_0805_2012Metric, F.Cu at (321.8, -15.4)
- added U2: BMP581, VELION_VCU_Library:BMP581, F.Cu at (316.7, 144.4)
- C108, C109, C110, C111, C133, C134, C139, C140, C141, C142, C143, C144, C151, C156, C251, C259, C282, C283: footprint Capacitor_SMD:C_0805_2012Metric -> VELION_VCU_Library:C_0805_2012Metric
- C112, C16, C18, C19: footprint Capacitor_SMD:C_1210_3225Metric -> VELION_VCU_Library:C_1210_3225Metric
- C113, C135, C136, C137, C138, C149, C15, C150, C152, C153, C154, C155, C17, C247, C250, C256, C257, C258, C260, C261, C262, C263, C264, C265, C266, C267, C268, C269, C270, C271, C284, C285, C292, C321: footprint Capacitor_SMD:C_0603_1608Metric -> VELION_VCU_Library:C_0603_1608Metric
- C20: footprint Capacitor_SMD:C_1206_3216Metric -> VELION_VCU_Library:C_1206_3216Metric
- C248, C249: footprint Capacitor_SMD:C_0402_1005Metric -> VELION_VCU_Library:C_0402_1005Metric
- D27: footprint Diode_SMD:D_SOD-123F -> VELION_VCU_Library:D_SOD-123F
- D28: footprint Package_TO_SOT_SMD:SOT-323_SC-70 -> VELION_VCU_Library:SOT-323_SC-70
- D29, D30: footprint Diode_SMD:D_SMA -> VELION_VCU_Library:D_SMA
- D5: footprint Package_TO_SOT_SMD:SOT-23 -> VELION_VCU_Library:SOT-23
- FID1, FID2, FID3, FID4, FID5, FID6: footprint Fiducial:Fiducial_1mm_Mask2mm -> VELION_VCU_Library:Fiducial_1mm_Mask2mm
- H1, H2, H3, H4, H5, H6: footprint MountingHole:MountingHole_3.2mm_M3 -> VELION_VCU_Library:MountingHole_3.2mm_M3
- IC2: footprint Package_DFN_QFN:QFN-24-1EP_4x4mm_P0.5mm_EP2.7x2.7mm -> VELION_VCU_Library:QFN-24-1EP_4x4mm_P0.5mm_EP2.7x2.7mm
- IC3, IC4: footprint E-M-IntegratedCircuits:SOIC127P600X175-9N -> VELION_VCU_Library:SOIC127P600X175-9N
- J15: footprint Connector_USB:USB_C_Receptacle_GCT_USB4110-GF-A -> VELION_VCU_Library:USB_C_Receptacle_GCT_USB4110-GF-A
- J4: footprint Connector_PinHeader_2.00mm:PinHeader_2x03_P2.00mm_Vertical_SMD -> VELION_VCU_Library:PinHeader_2x03_P2.00mm_Vertical_SMD
- J7: footprint Connector_Amphenol:Amphenol_M8S-03PMMR-SF8001 -> VELION_VCU_Library:Amphenol_M8S-03PMMR-SF8001
- L12, L13: footprint Inductor_SMD:L_APV_APH0850 -> VELION_VCU_Library:L_APV_APH0850
- L15, L16: footprint Inductor_SMD:L_APV_APH0650 -> VELION_VCU_Library:L_APV_APH0650
- L24, L3: footprint Inductor_SMD:L_1210_3225Metric -> VELION_VCU_Library:L_1210_3225Metric
- Q6, Q7: footprint Package_SON:Diodes_PowerDI3333-8 -> VELION_VCU_Library:Diodes_PowerDI3333-8
- R10: footprint Resistor_SMD:R_1206_3216Metric -> VELION_VCU_Library:R_1206_3216Metric
- R11, R116, R117, R118, R119, R12, R120, R121, R122, R123, R124, R125, R144, R145, R146, R147, R148, R149, R150, R151, R208, R209, R210, R211, R212, R216, R217, R218, R219, R220, R226, R227, R228, R233, R234, R263, R264, R8, R9: footprint Resistor_SMD:R_0603_1608Metric -> VELION_VCU_Library:R_0603_1608Metric
- R111: footprint Resistor_SMD:R_0805_2012Metric -> VELION_VCU_Library:R_0805_2012Metric
- TP11, TP2: footprint TestPoint:TestPoint_THTPad_D1.5mm_Drill0.7mm -> VELION_VCU_Library:TestPoint_THTPad_D1.5mm_Drill0.7mm
- TP12, TP13, TP14, TP22, TP23, TP28: footprint TestPoint:TestPoint_Pad_D1.5mm -> VELION_VCU_Library:TestPoint_Pad_D1.5mm
- U1: footprint Package_QFP:LQFP-144_20x20mm_P0.5mm -> VELION_VCU_Library:LQFP-144_20x20mm_P0.5mm
- U10, U11, U12, U13, U14, U15, U3, U5, U6, U7, U8, U9: footprint Package_SO:PowerSSO-16-1EP_3.9x4.9mm_P0.5mm_EP2.5x3.61mm -> VELION_VCU_Library:PowerSSO-16-1EP_3.9x4.9mm_P0.5mm_EP2.5x3.61mm
- U27: footprint Package_TO_SOT_SMD:SOT-666 -> VELION_VCU_Library:SOT-666
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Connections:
- U10 pad 1: /BackLightsControl/RearDirLampL -> Net-(U10-INPUT0)
- U10 pad 3: /BackLightsControl/selH -> Net-(U10-SEn)
- U10 pad 8: /BackLightsControl/StopLamp -> Net-(U10-INPUT1)
- U11 pad 1: /BackLightsControl/RearPosLamp -> Net-(U11-INPUT0)
- U11 pad 3: /BackLightsControl/selI -> Net-(U11-SEn)
- U11 pad 8: /BackLightsControl/RearFogLamp -> Net-(U11-INPUT1)
- U12 pad 1: /BackLightsControl/ReversingLamp -> Net-(U12-INPUT0)
- U12 pad 3: /BackLightsControl/selJ -> Net-(U12-SEn)
- U13 pad 1: /Reserved2 -> Net-(U13-INPUT0)
- U13 pad 3: /BackLightsControl/selK -> Net-(U13-SEn)
- U13 pad 8: /BackLightsControl/DirIndicatorL -> Net-(U13-INPUT1)
- U14 pad 1: /BackLightsControl/DrivingBeam -> Net-(U14-INPUT0)
- U14 pad 3: /BackLightsControl/selL -> Net-(U14-SEn)
- U14 pad 8: /BackLightsControl/DirIndicatorR -> Net-(U14-INPUT1)
- U15 pad 1: /MCU/SideMarkLampL -> Net-(U15-INPUT0)
- U15 pad 3: /MCU/selF -> Net-(U15-SEn)
- U15 pad 8: /MCU/SideDirLampL -> Net-(U15-INPUT1)
- U3 pad 1: /FrontLightsControl/FrontPosLamp -> Net-(U3-INPUT0)
- U3 pad 3: /FrontLightsControl/selA -> Net-(U3-SEn)
- U3 pad 8: /FrontLightsControl/FrontDirLampR -> Net-(U3-INPUT1)
- U5 pad 1: /FrontLightsControl/FrontDirLampL -> Net-(U5-INPUT0)
- U5 pad 3: /FrontLightsControl/selB -> Net-(U5-SEn)
- U5 pad 8: /FrontLightsControl/PassingBeamLamp -> Net-(U5-INPUT1)
- U6 pad 1: /FrontLightsControl/DrivingBeamLamp -> Net-(U6-INPUT0)
- U6 pad 3: /FrontLightsControl/selC -> Net-(U6-SEn)
- U6 pad 8: /FrontLightsControl/DaytimeLamp -> Net-(U6-INPUT1)
- U7 pad 1: /FrontLightsControl/AudibleWarn -> Net-(U7-INPUT0)
- U7 pad 3: /FrontLightsControl/selD -> Net-(U7-SEn)
- U7 pad 8: /Reserved3 -> Net-(U7-INPUT1)
- U8 pad 1: /MCU/SideMarkLampR -> Net-(U8-INPUT0)
- U8 pad 3: /MCU/selE -> Net-(U8-SEn)
- U8 pad 8: /MCU/SideDirLampR -> Net-(U8-INPUT1)
- U9 pad 1: /BackLightsControl/CargoCompLamp -> Net-(U9-INPUT0)
- U9 pad 3: /BackLightsControl/selG -> Net-(U9-SEn)
- U9 pad 8: /BackLightsControl/RearDirLampR -> Net-(U9-INPUT1)
- Y6 pad 2: Net-(U1PortG_PORTH-PC14) -> unconnected-(Y6-Pad2)
